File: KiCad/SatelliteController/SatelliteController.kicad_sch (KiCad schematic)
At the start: 33 parts, among them J1 CONN_ICSP, J2 CONN_USB, J3 USB_B_Micro, SW1 SW_RESET, U1 FT232RL, U2 ATMEGA2560-16AUR, Y1 HUSG-16.000-20

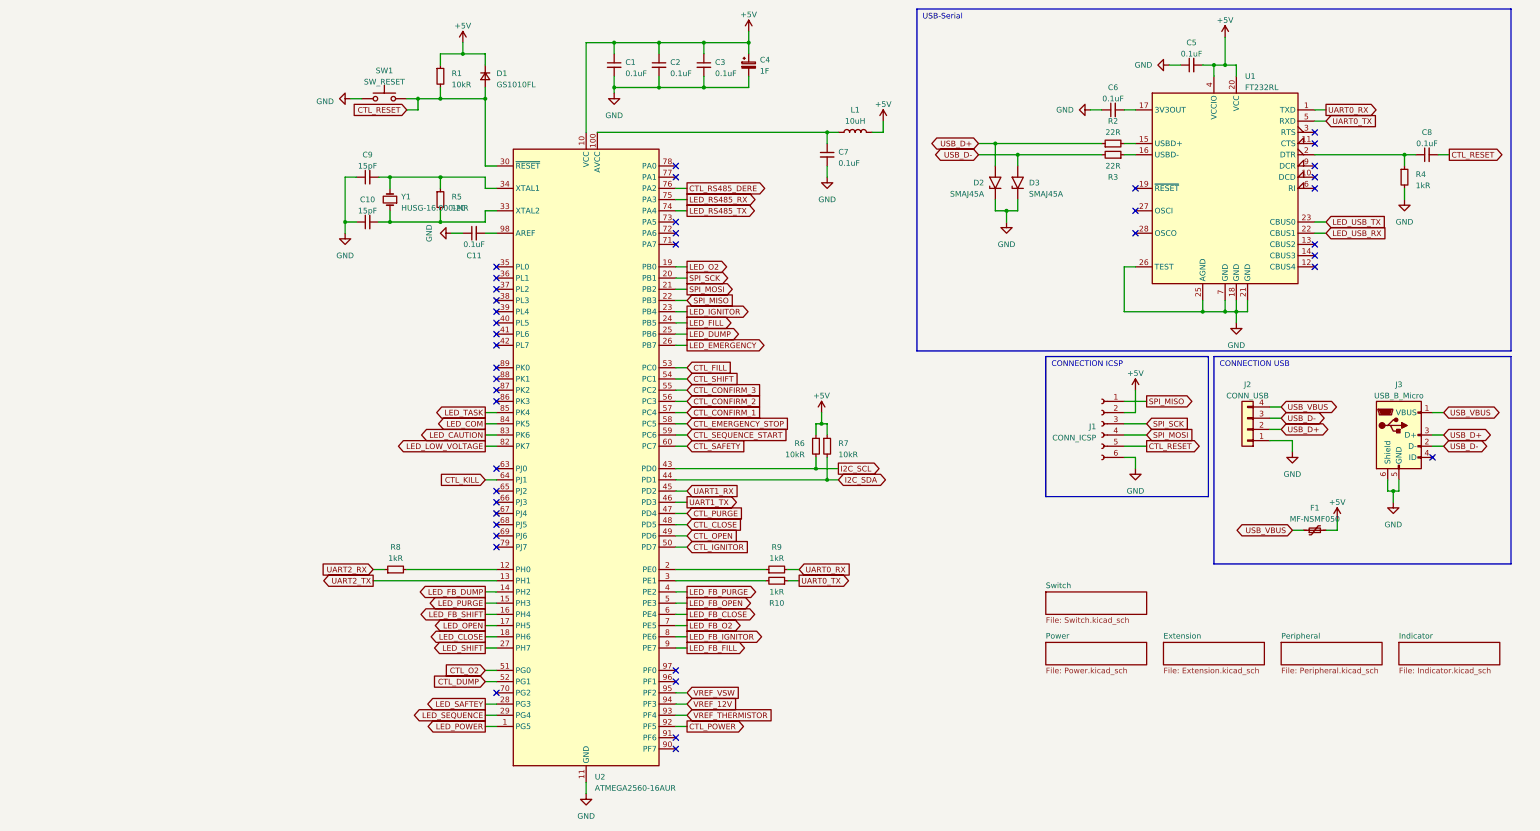
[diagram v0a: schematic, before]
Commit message: 圧力センサとの接続部を追加
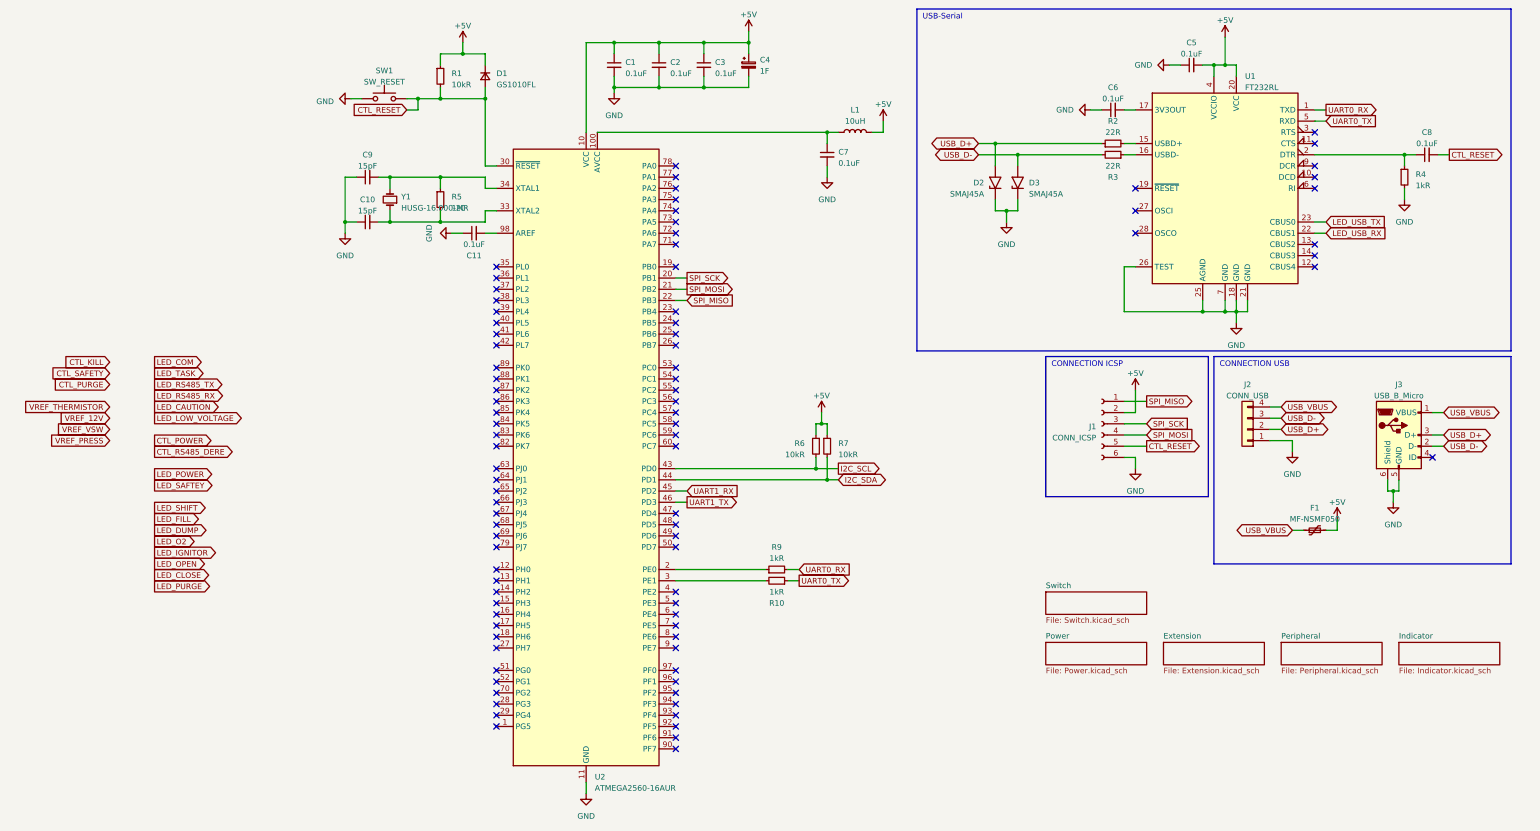
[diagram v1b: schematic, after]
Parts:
- removed R8: 1kR, Resistor_SMD:R_0603_1608Metric_Pad0.98x0.95mm_HandSolder, symbol Device:R_Small
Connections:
- net CTL_KILL: no longer U2.64 (PJ1)
- net CTL_POWER: no longer U2.92 (PF5)
- net CTL_PURGE: no longer U2.47 (PD4)
- net CTL_RS485_DERE: no longer U2.76 (PA2)
- net CTL_SAFETY: no longer U2.60 (PC7)
- net LED_CAUTION: no longer U2.83 (PK6)
- net LED_CLOSE: no longer U2.18 (PH6)
- net LED_COM: no longer U2.84 (PK5)
- net LED_DUMP: no longer U2.25 (PB6)
- net LED_FILL: no longer U2.24 (PB5)
- net LED_IGNITOR: no longer U2.23 (PB4)
- net LED_LOW_VOLTAGE: no longer U2.82 (PK7)
- net LED_O2: no longer U2.19 (PB0)
- net LED_OPEN: no longer U2.17 (PH5)
- net LED_POWER: no longer U2.1 (PG5)
- net LED_PURGE: no longer U2.15 (PH3)
- net LED_RS485_RX: no longer U2.75 (PA3)
- net LED_RS485_TX: no longer U2.74 (PA4)
- net LED_SAFTEY: no longer U2.28 (PG3)
- net LED_SHIFT: no longer U2.27 (PH7)
- net LED_TASK: no longer U2.85 (PK4)
- net VREF_12V: no longer U2.94 (PF3)
- net VREF_THERMISTOR: no longer U2.93 (PF4)
- net VREF_VSW: no longer U2.95 (PF2)
- net CTL_CLOSE: no longer names the net of U2.48 (PD5)
- net CTL_CONFIRM_1: no longer names the net of U2.57 (PC4)
- net CTL_CONFIRM_2: no longer names the net of U2.56 (PC3)
- net CTL_CONFIRM_3: no longer names the net of U2.55 (PC2)
- net CTL_DUMP: no longer names the net of U2.52 (PG1)
- net CTL_EMERGENCY_STOP: no longer names the net of U2.58 (PC5)
- net CTL_FILL: no longer names the net of U2.53 (PC0)
- net CTL_IGNITOR: no longer names the net of U2.50 (PD7)
- net CTL_O2: no longer names the net of U2.51 (PG0)
- net CTL_OPEN: no longer names the net of U2.49 (PD6)
- net CTL_SEQUENCE_START: no longer names the net of U2.59 (PC6)
- net CTL_SHIFT: no longer names the net of U2.54 (PC1)
- net LED_EMERGENCY: no longer names the net of U2.26 (PB7)
- net LED_FB_CLOSE: no longer names the net of U2.6 (PE4)
- net LED_FB_DUMP: no longer names the net of U2.14 (PH2)
- net LED_FB_FILL: no longer names the net of U2.9 (PE7)
- net LED_FB_IGNITOR: no longer names the net of U2.8 (PE6)
- net LED_FB_O2: no longer names the net of U2.7 (PE5)
- net LED_FB_OPEN: no longer names the net of U2.5 (PE3)
- net LED_FB_PURGE: no longer names the net of U2.4 (PE2)
- net LED_FB_SHIFT: no longer names the net of U2.16 (PH4)
- net LED_SEQUENCE: no longer names the net of U2.29 (PG4)
- net UART2_TX: no longer names the net of U2.13 (PH1)
- no-connect marks 41 -> 89

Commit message: ランコンのKiCadプロジェクトをコピーしてサテコンを作成
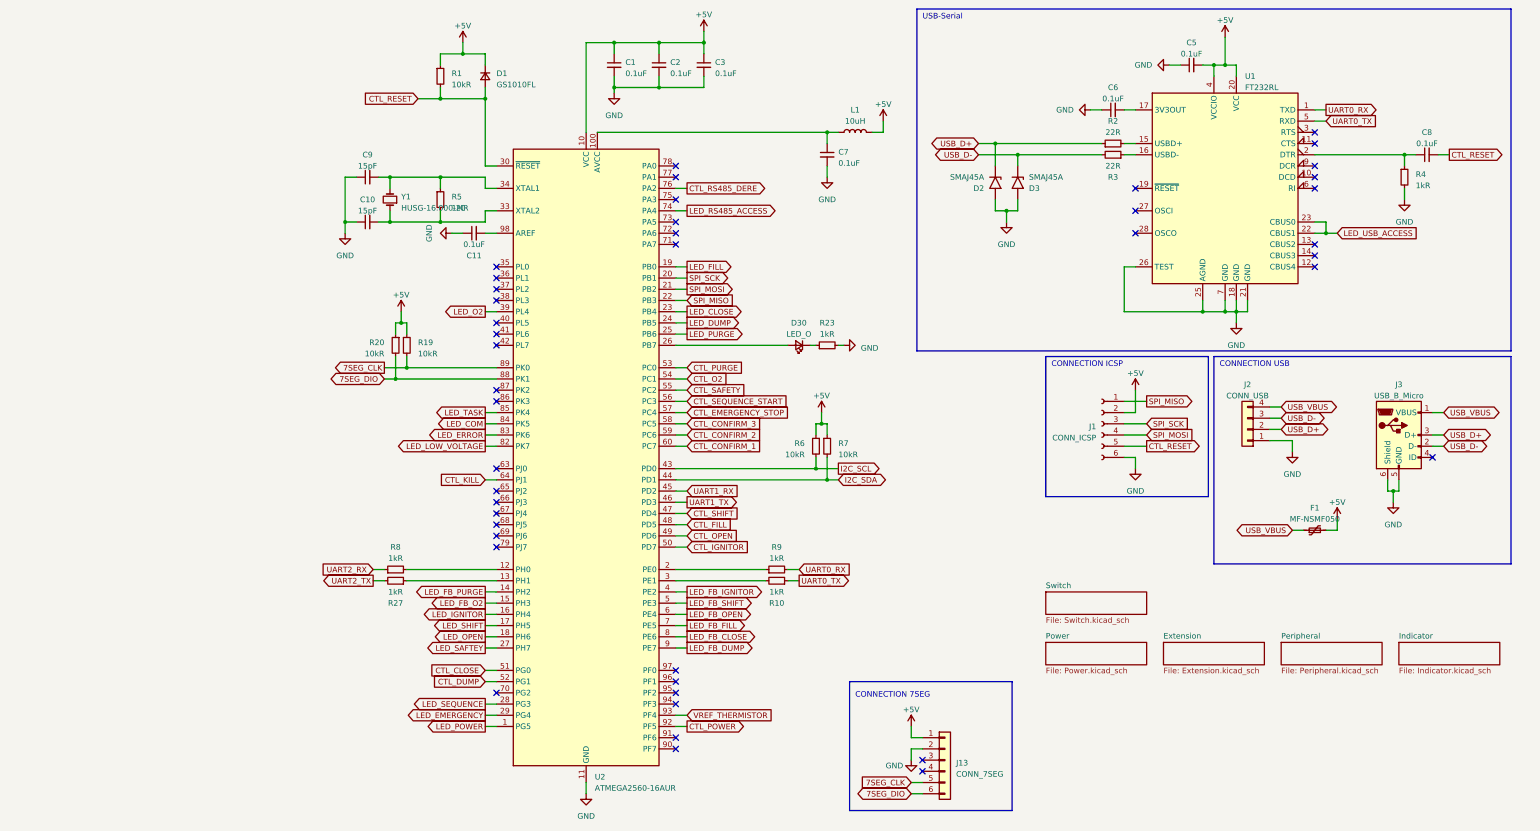
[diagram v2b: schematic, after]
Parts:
- removed C4: 1F, Capacitor_THT:DX_5R5VxxxxU_D19.0mm_P5.00mm, symbol Device:C_Polarized_Small
- removed SW1: SW_RESET, Button_Switch_THT:SW_PUSH_6mm_H7.3mm, symbol Switch:SW_Push
- added D30: LED_O, LED_SMD:LED_0603_1608Metric_Pad1.05x0.95mm_HandSolder, symbol Device:LED_Small
- added J13: CONN_7SEG, TSRP_Connector_Hirose:DF51A-6DP-2DSA, symbol Connector_Generic:Conn_01x06
- added R19, R20: 10kR, Resistor_SMD:R_0603_1608Metric_Pad0.98x0.95mm_HandSolder, symbol Device:R_Small
- added R23, R27, R8: 1kR, Resistor_SMD:R_0603_1608Metric_Pad0.98x0.95mm_HandSolder, symbol Device:R_Small
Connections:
- net LED_USB_TX is gone; now on net LED_USB_ACCESS: U1.23 (CBUS0)
- net +5V: now also J13.1 (Pin_1), R19.1, R20.1
- net CTL_KILL: now also U2.64 (PJ1)
- net CTL_POWER: now also U2.92 (PF5)
- net CTL_PURGE: now also U2.53 (PC0)
- net CTL_RS485_DERE: now also U2.76 (PA2)
- net CTL_SAFETY: now also U2.55 (PC2)
- net GND: now also D2.2 (A2), D3.2 (A2), J13.2 (Pin_2), R23.2; no longer D2.1 (A1), D3.1 (A1)
- net LED_CLOSE: now also U2.23 (PB4)
- net LED_COM: now also U2.84 (PK5)
- net LED_DUMP: now also U2.24 (PB5)
- net LED_FILL: now also U2.19 (PB0)
- net LED_IGNITOR: now also U2.16 (PH4)
- net LED_LOW_VOLTAGE: now also U2.82 (PK7)
- net LED_O2: now also U2.39 (PL4)
- net LED_OPEN: now also U2.18 (PH6)
- net LED_POWER: now also U2.1 (PG5)
- net LED_PURGE: now also U2.25 (PB6)
- net LED_SAFTEY: now also U2.27 (PH7)
- net LED_SHIFT: now also U2.17 (PH5)
- net LED_TASK: now also U2.85 (PK4)
- net USB_D+: now also D2.1 (A1); no longer D2.2 (A2)
- net USB_D-: now also D3.1 (A1); no longer D3.2 (A2)
- net VREF_THERMISTOR: now also U2.93 (PF4)
- net at U2.12 (PH0): now also R8.2
- net at U2.13 (PH1): now also R27.1
- net LED_FB_PURGE: now reaches U2.14 (PH2)
- net LED_FB_O2: now reaches U2.15 (PH3)
- net at U2.26 (PB7): now also D30.2 (A)
- net LED_SEQUENCE: now reaches U2.28 (PG3)
- net LED_EMERGENCY: now reaches U2.29 (PG4)
- net LED_FB_IGNITOR: now reaches U2.4 (PE2)
- net CTL_SHIFT: now reaches U2.47 (PD4)
- net CTL_FILL: now reaches U2.48 (PD5)
- net CTL_OPEN: now reaches U2.49 (PD6)
- net LED_FB_SHIFT: now reaches U2.5 (PE3)
- net CTL_IGNITOR: now reaches U2.50 (PD7)
- net CTL_CLOSE: now reaches U2.51 (PG0)
- net CTL_DUMP: now reaches U2.52 (PG1)
- net CTL_O2: now reaches U2.54 (PC1)
- net CTL_SEQUENCE_START: now reaches U2.56 (PC3)
- net CTL_EMERGENCY_STOP: now reaches U2.57 (PC4)
- net CTL_CONFIRM_3: now reaches U2.58 (PC5)
- net CTL_CONFIRM_2: now reaches U2.59 (PC6)
- net LED_FB_OPEN: now reaches U2.6 (PE4)
- net CTL_CONFIRM_1: now reaches U2.60 (PC7)
- net LED_FB_FILL: now reaches U2.7 (PE5)
- net LED_RS485_ACCESS: now reaches U2.74 (PA4)
- net LED_FB_CLOSE: now reaches U2.8 (PE6)
- net LED_ERROR: now reaches U2.83 (PK6)
- net 7SEG_DIO: now reaches U2.88 (PK1)
- net 7SEG_DIO: now also J13.6 (Pin_6), R20.2
- net 7SEG_CLK: now reaches U2.89 (PK0)
- net 7SEG_CLK: now also J13.5 (Pin_5), R19.2
- net LED_FB_DUMP: now reaches U2.9 (PE7)
- net LED_USB_RX renamed LED_USB_ACCESS
- new net: D30.1 (K), R23.1
- new net UART2_RX: R8.1
- new net UART2_TX: R27.2
- no-connect marks 89 -> 43
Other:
- note added: "CONNECTION 7SEG"
- company: (none) -> Tokai Student Rocket Project
- title: (none) -> GSE Gen 6 Launch Controller

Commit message: 音声完成を削除
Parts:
- removed R27, R8: 1kR, Resistor_SMD:R_0603_1608Metric_Pad0.98x0.95mm_HandSolder, symbol Device:R_Small
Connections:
- no-connect marks 43 -> 45
